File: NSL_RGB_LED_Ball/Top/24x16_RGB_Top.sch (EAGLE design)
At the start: 20 parts

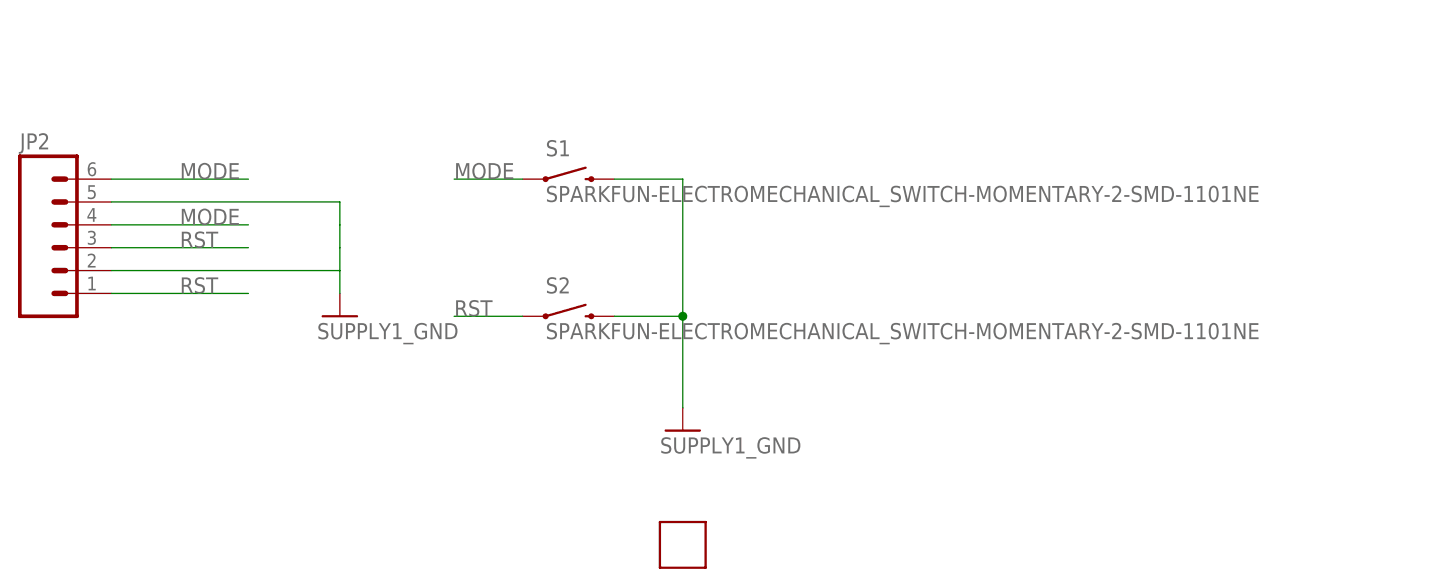
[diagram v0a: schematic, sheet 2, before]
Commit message: 
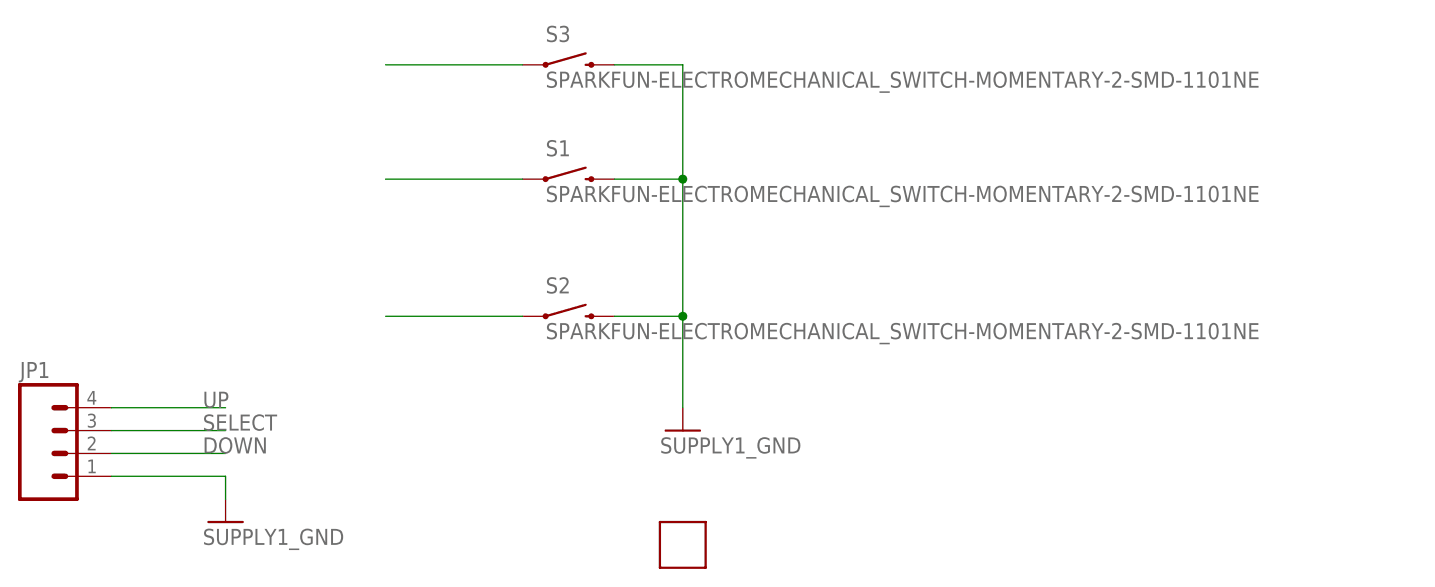
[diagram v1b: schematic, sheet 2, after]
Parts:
- removed JP2: (no value), SparkFun-Connectors:M06SIP
- added JP1: (no value), SparkFun-Connectors:M04PTH
- added S3: SPARKFUN-ELECTROMECHANICAL_SWITCH-MOMENTARY-2-SMD-1101NE, tvbgone-2layer:SPARKFUN-ELECTROMECHANICAL_SWITCH-MOMENTARY-2-SMD-1101NE
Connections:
- removed net MODE: JP2.4, JP2.6, S1.1
- removed net RST: JP2.1, JP2.3, S2.1
- new net DOWN: JP1.2, S2.1
- new net SELECT: JP1.3, S1.1
- new net UP: JP1.4, S3.1
- net GND: now also JP1.1, S3.2; no longer JP2.2, JP2.5
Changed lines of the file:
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@@
 <part name="S1" library="tvbgone-2layer" deviceset="SPARKFUN-ELECTROMECHANICAL_SWITCH-MOMENTARY-2" device="-SMD-1101NE"/>
 <part name="S2" library="tvbgone-2layer" deviceset="SPARKFUN-ELECTROMECHANICAL_SWITCH-MOMENTARY-2" device="-SMD-1101NE"/>
-<part name="GND1" library="tvbgone-2layer" deviceset="SUPPLY1_GND" device=""/>
 <part name="GND2" library="tvbgone-2layer" deviceset="SUPPLY1_GND" device=""/>
-<part name="JP2" library="SparkFun-Connectors" deviceset="M06" device="SIP"/>
 <part name="U$1" library="24x16_RGB_Bottom" deviceset="USB_PANNEL" device=""/>
+<part name="JP1" library="SparkFun-Connectors" deviceset="M04" device="PTH"/>
+<part name="GND3" library="tvbgone-2layer" deviceset="SUPPLY1_GND" device=""/>
+<part name="S3" library="tvbgone-2layer" deviceset="SPARKFUN-ELECTROMECHANICAL_SWITCH-MOMENTARY-2" device="-SMD-1101NE"/>
 </parts>
 <sheets>
@@
 <instance part="S1" gate="G$1" x="55.88" y="81.28"/>
 <instance part="S2" gate="G$1" x="55.88" y="66.04"/>
-<instance part="GND1" gate="1" x="30.48" y="66.04"/>
 <instance part="GND2" gate="1" x="68.58" y="53.34"/>
-<instance part="JP2" gate="G$1" x="0" y="73.66"/>
 <instance part="U$1" gate="G$1" x="68.58" y="40.64"/>
+<instance part="JP1" gate="G$1" x="0" y="50.8"/>
+<instance part="GND3" gate="1" x="17.78" y="43.18"/>
+<instance part="S3" gate="G$1" x="55.88" y="93.98"/>
 </instances>
 <busses>
 </busses>
 <nets>
-<net name="MODE" class="0">
-<segment>
-<pinref part="S1" gate="G$1" pin="1"/>
-<wire x1="50.8" y1="81.28" x2="43.18" y2="81.28" width="0.1524" layer="91"/>
-<label x="43.18" y="81.28" size="1.778" layer="95"/>
-</segment>
-<segment>
-<wire x1="5.08" y1="81.28" x2="20.32" y2="81.28" width="0.1524" layer="91"/>
-<label x="12.7" y="81.28" size="1.778" layer="95"/>
-<pinref part="JP2" gate="G$1" pin="6"/>
-</segment>
-<segment>
-<wire x1="5.08" y1="76.2" x2="20.32" y2="76.2" width="0.1524" layer="91"/>
-<pinref part="JP2" gate="G$1" pin="4"/>
-<label x="12.7" y="76.2" size="1.778" layer="95"/>
-</segment>
-</net>
-<net name="RST" class="0">
-<segment>
-<pinref part="S2" gate="G$1" pin="1"/>
-<wire x1="50.8" y1="66.04" x2="43.18" y2="66.04" width="0.1524" layer="91"/>
-<label x="43.18" y="66.04" size="1.778" layer="95"/>
-</segment>
-<segment>
-<wire x1="5.08" y1="68.58" x2="20.32" y2="68.58" width="0.1524" layer="91"/>
-<label x="12.7" y="68.58" size="1.778" layer="95"/>
-<pinref part="JP2" gate="G$1" pin="1"/>
-</segment>
-<segment>
-<wire x1="5.08" y1="73.66" x2="20.32" y2="73.66" width="0.1524" layer="91"/>
-<pinref part="JP2" gate="G$1" pin="3"/>
-<label x="12.7" y="73.66" size="1.778" layer="95"/>
-</segment>
-</net>
 <net name="GND" class="0">
-<segment>
-<wire x1="30.48" y1="76.2" x2="30.48" y2="73.66" width="0.1524" layer="91"/>
-<wire x1="30.48" y1="73.66" x2="30.48" y2="71.12" width="0.1524" layer="91"/>
-<wire x1="30.48" y1="71.12" x2="30.48" y2="68.58" width="0.1524" layer="91"/>
-<pinref part="GND1" gate="1" pin="GND"/>
-<pinref part="JP2" gate="G$1" pin="5"/>
-<wire x1="5.08" y1="78.74" x2="30.48" y2="78.74" width="0.1524" layer="91"/>
-<wire x1="30.48" y1="78.74" x2="30.48" y2="76.2" width="0.1524" layer="91"/>
-<pinref part="JP2" gate="G$1" pin="2"/>
-<wire x1="5.08" y1="71.12" x2="30.48" y2="71.12" width="0.1524" layer="91"/>
-</segment>
 <segment>
 <pinref part="S1" gate="G$1" pin="2"/>
@@
 <junction x="68.58" y="66.04"/>
 <pinref part="GND2" gate="1" pin="GND"/>
-</segment>
-</net>
+<pinref part="S3" gate="G$1" pin="2"/>
+<wire x1="60.96" y1="93.98" x2="68.58" y2="93.98" width="0.1524" layer="91"/>
+<wire x1="68.58" y1="93.98" x2="68.58" y2="81.28" width="0.1524" layer="91"/>
+<junction x="68.58" y="81.28"/>
+</segment>
+<segment>
+<pinref part="JP1" gate="G$1" pin="1"/>
+<wire x1="5.08" y1="48.26" x2="17.78" y2="48.26" width="0.1524" layer="91"/>
+<pinref part="GND3" gate="1" pin="GND"/>
+<wire x1="17.78" y1="48.26" x2="17.78" y2="45.72" width="0.1524" layer="91"/>
+</segment>
+</net>
+<net name="UP" class="0">
+<segment>
+<pinref part="JP1" gate="G$1" pin="4"/>
+<wire x1="5.08" y1="55.88" x2="17.78" y2="55.88" width="0.1524" layer="91"/>
+<label x="15.24" y="55.88" size="1.778" layer="95"/>
+</segment>
+<segment>
+<wire x1="35.56" y1="93.98" x2="50.8" y2="93.98" width="0.1524" layer="91"/>
+<pinref part="S3" gate="G$1" pin="1"/>
+</segment>
+</net>
+<net name="SELECT" class="0">
+<segment>
+<pinref part="JP1" gate="G$1" pin="3"/>
+<wire x1="5.08" y1="53.34" x2="17.78" y2="53.34" width="0.1524" layer="91"/>
+<label x="15.24" y="53.34" size="1.778" layer="95"/>
+</segment>
+<segment>
+<wire x1="35.56" y1="81.28" x2="50.8" y2="81.28" width="0.1524" layer="91"/>
+<pinref part="S1" gate="G$1" pin="1"/>
+</segment>
+</net>
+<net name="DOWN" class="0">
+<segment>
+<pinref part="JP1" gate="G$1" pin="2"/>
+<wire x1="5.08" y1="50.8" x2="17.78" y2="50.8" width="0.1524" layer="91"/>
+<label x="15.24" y="50.8" size="1.778" layer="95"/>
+</segment>
+<segment>
+<wire x1="35.56" y1="66.04" x2="50.8" y2="66.04" width="0.1524" layer="91"/>
+<pinref part="S2" gate="G$1" pin="1"/>
+</segment>
+</net>

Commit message: 
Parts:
- SLOT1, SLOT10, SLOT11, SLOT12, SLOT13, SLOT14, SLOT15, SLOT16, SLOT2, SLOT3, SLOT4, SLOT5, SLOT6, SLOT7, SLOT8, SLOT9: device 24x16_RGB_Bottom:SLOT -> 24x16_RGB_Top:SLOT
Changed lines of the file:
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@@
 </classes>
 <parts>
-<part name="SLOT1" library="24x16_RGB_Bottom" deviceset="SLOT" device="">
+<part name="SLOT1" library="24x16_RGB_Top" deviceset="SLOT" device="">
 <attribute name="MF" value=""/>
 <attribute name="MPN" value=""/>
 <attribute name="OC_NEWARK" value="unknown"/>
 </part>
-<part name="SLOT2" library="24x16_RGB_Bottom" deviceset="SLOT" device="">
+<part name="SLOT2" library="24x16_RGB_Top" deviceset="SLOT" device="">
 <attribute name="MF" value=""/>
 <attribute name="MPN" value=""/>
 <attribute name="OC_NEWARK" value="unknown"/>
 </part>
-<part name="SLOT3" library="24x16_RGB_Bottom" deviceset="SLOT" device="">
+<part name="SLOT3" library="24x16_RGB_Top" deviceset="SLOT" device="">
 <attribute name="MF" value=""/>
 <attribute name="MPN" value=""/>
 <attribute name="OC_NEWARK" value="unknown"/>
 </part>
-<part name="SLOT4" library="24x16_RGB_Bottom" deviceset="SLOT" device="">
+<part name="SLOT4" library="24x16_RGB_Top" deviceset="SLOT" device="">
 <attribute name="MF" value=""/>
 <attribute name="MPN" value=""/>
 <attribute name="OC_NEWARK" value="unknown"/>
 </part>
-<part name="SLOT5" library="24x16_RGB_Bottom" deviceset="SLOT" device="">
+<part name="SLOT5" library="24x16_RGB_Top" deviceset="SLOT" device="">
 <attribute name="MF" value=""/>
 <attribute name="MPN" value=""/>
 <attribute name="OC_NEWARK" value="unknown"/>
 </part>
-<part name="SLOT6" library="24x16_RGB_Bottom" deviceset="SLOT" device="">
+<part name="SLOT6" library="24x16_RGB_Top" deviceset="SLOT" device="">
 <attribute name="MF" value=""/>
 <attribute name="MPN" value=""/>
 <attribute name="OC_NEWARK" value="unknown"/>
 </part>
-<part name="SLOT7" library="24x16_RGB_Bottom" deviceset="SLOT" device="">
+<part name="SLOT7" library="24x16_RGB_Top" deviceset="SLOT" device="">
 <attribute name="MF" value=""/>
 <attribute name="MPN" value=""/>
 <attribute name="OC_NEWARK" value="unknown"/>
 </part>
-<part name="SLOT8" library="24x16_RGB_Bottom" deviceset="SLOT" device="">
+<part name="SLOT8" library="24x16_RGB_Top" deviceset="SLOT" device="">
 <attribute name="MF" value=""/>
 <attribute name="MPN" value=""/>
 <attribute name="OC_NEWARK" value="unknown"/>
 </part>
-<part name="SLOT9" library="24x16_RGB_Bottom" deviceset="SLOT" device="">
+<part name="SLOT9" library="24x16_RGB_Top" deviceset="SLOT" device="">
 <attribute name="MF" value=""/>
 <attribute name="MPN" value=""/>
 <attribute name="OC_NEWARK" value="unknown"/>
 </part>
-<part name="SLOT10" library="24x16_RGB_Bottom" deviceset="SLOT" device="">
+<part name="SLOT10" library="24x16_RGB_Top" deviceset="SLOT" device="">
 <attribute name="MF" value=""/>
 <attribute name="MPN" value=""/>
 <attribute name="OC_NEWARK" value="unknown"/>
 </part>
-<part name="SLOT11" library="24x16_RGB_Bottom" deviceset="SLOT" device="">
+<part name="SLOT11" library="24x16_RGB_Top" deviceset="SLOT" device="">
 <attribute name="MF" value=""/>
 <attribute name="MPN" value=""/>
 <attribute name="OC_NEWARK" value="unknown"/>
 </part>
-<part name="SLOT12" library="24x16_RGB_Bottom" deviceset="SLOT" device="">
+<part name="SLOT12" library="24x16_RGB_Top" deviceset="SLOT" device="">
 <attribute name="MF" value=""/>
 <attribute name="MPN" value=""/>
 <attribute name="OC_NEWARK" value="unknown"/>
 </part>
-<part name="SLOT13" library="24x16_RGB_Bottom" deviceset="SLOT" device="">
+<part name="SLOT13" library="24x16_RGB_Top" deviceset="SLOT" device="">
 <attribute name="MF" value=""/>
 <attribute name="MPN" value=""/>
 <attribute name="OC_NEWARK" value="unknown"/>
 </part>
-<part name="SLOT14" library="24x16_RGB_Bottom" deviceset="SLOT" device="">
+<part name="SLOT14" library="24x16_RGB_Top" deviceset="SLOT" device="">
 <attribute name="MF" value=""/>
 <attribute name="MPN" value=""/>
 <attribute name="OC_NEWARK" value="unknown"/>
 </part>
-<part name="SLOT15" library="24x16_RGB_Bottom" deviceset="SLOT" device="">
+<part name="SLOT15" library="24x16_RGB_Top" deviceset="SLOT" device="">
 <attribute name="MF" value=""/>
 <attribute name="MPN" value=""/>
 <attribute name="OC_NEWARK" value="unknown"/>
 </part>
-<part name="SLOT16" library="24x16_RGB_Bottom" deviceset="SLOT" device="">
+<part name="SLOT16" library="24x16_RGB_Top" deviceset="SLOT" device="">
 <attribute name="MF" value=""/>
 <attribute name="MPN" value=""/>

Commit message: 
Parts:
- removed JP1: (no value), SparkFun-Connectors:M04PTH
- added JP2: (no value), SparkFun-Connectors:M06SIP
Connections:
- net DOWN: now also JP2.4; no longer JP1.2
- net GND: now also JP2.1, JP2.2, JP2.3; no longer JP1.1
- net SELECT: now also JP2.5; no longer JP1.3
- net UP: now also JP2.6; no longer JP1.4
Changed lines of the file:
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@@
 <part name="GND2" library="tvbgone-2layer" deviceset="SUPPLY1_GND" device=""/>
 <part name="U$1" library="24x16_RGB_Bottom" deviceset="USB_PANNEL" device=""/>
-<part name="JP1" library="SparkFun-Connectors" deviceset="M04" device="PTH"/>
 <part name="GND3" library="tvbgone-2layer" deviceset="SUPPLY1_GND" device=""/>
 <part name="S3" library="tvbgone-2layer" deviceset="SPARKFUN-ELECTROMECHANICAL_SWITCH-MOMENTARY-2" device="-SMD-1101NE"/>
+<part name="JP2" library="SparkFun-Connectors" deviceset="M06" device="SIP"/>
 </parts>
 <sheets>
@@
 <instance part="GND2" gate="1" x="68.58" y="53.34"/>
 <instance part="U$1" gate="G$1" x="68.58" y="40.64"/>
-<instance part="JP1" gate="G$1" x="0" y="50.8"/>
-<instance part="GND3" gate="1" x="17.78" y="43.18"/>
+<instance part="GND3" gate="1" x="25.4" y="43.18"/>
 <instance part="S3" gate="G$1" x="55.88" y="93.98"/>
+<instance part="JP2" gate="G$1" x="0" y="48.26"/>
 </instances>
 <busses>
@@
 </segment>
 <segment>
-<pinref part="JP1" gate="G$1" pin="1"/>
-<wire x1="5.08" y1="48.26" x2="17.78" y2="48.26" width="0.1524" layer="91"/>
+<wire x1="5.08" y1="48.26" x2="25.4" y2="48.26" width="0.1524" layer="91"/>
 <pinref part="GND3" gate="1" pin="GND"/>
-<wire x1="17.78" y1="48.26" x2="17.78" y2="45.72" width="0.1524" layer="91"/>
+<wire x1="25.4" y1="48.26" x2="25.4" y2="45.72" width="0.1524" layer="91"/>
+<pinref part="JP2" gate="G$1" pin="3"/>
+<pinref part="JP2" gate="G$1" pin="2"/>
+<wire x1="5.08" y1="45.72" x2="20.32" y2="45.72" width="0.1524" layer="91"/>
+<pinref part="JP2" gate="G$1" pin="1"/>
+<wire x1="20.32" y1="45.72" x2="25.4" y2="45.72" width="0.1524" layer="91"/>
+<wire x1="5.08" y1="43.18" x2="20.32" y2="43.18" width="0.1524" layer="91"/>
+<wire x1="20.32" y1="43.18" x2="20.32" y2="45.72" width="0.1524" layer="91"/>
 </segment>
 </net>
 <net name="UP" class="0">
 <segment>
-<pinref part="JP1" gate="G$1" pin="4"/>
 <wire x1="5.08" y1="55.88" x2="17.78" y2="55.88" width="0.1524" layer="91"/>
 <label x="15.24" y="55.88" size="1.778" layer="95"/>
+<pinref part="JP2" gate="G$1" pin="6"/>
 </segment>
 <segment>
@@
 <net name="SELECT" class="0">
 <segment>
-<pinref part="JP1" gate="G$1" pin="3"/>
 <wire x1="5.08" y1="53.34" x2="17.78" y2="53.34" width="0.1524" layer="91"/>
 <label x="15.24" y="53.34" size="1.778" layer="95"/>
+<pinref part="JP2" gate="G$1" pin="5"/>
 </segment>
 <segment>
@@
 <net name="DOWN" class="0">
 <segment>
-<pinref part="JP1" gate="G$1" pin="2"/>
 <wire x1="5.08" y1="50.8" x2="17.78" y2="50.8" width="0.1524" layer="91"/>
 <label x="15.24" y="50.8" size="1.778" layer="95"/>
-</segment>
-<segment>
+<pinref part="JP2" gate="G$1" pin="4"/>
+</segment>
+<segment>
